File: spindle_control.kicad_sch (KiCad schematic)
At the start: 15 parts, among them U27 EL357N-G, U28 LM358DR

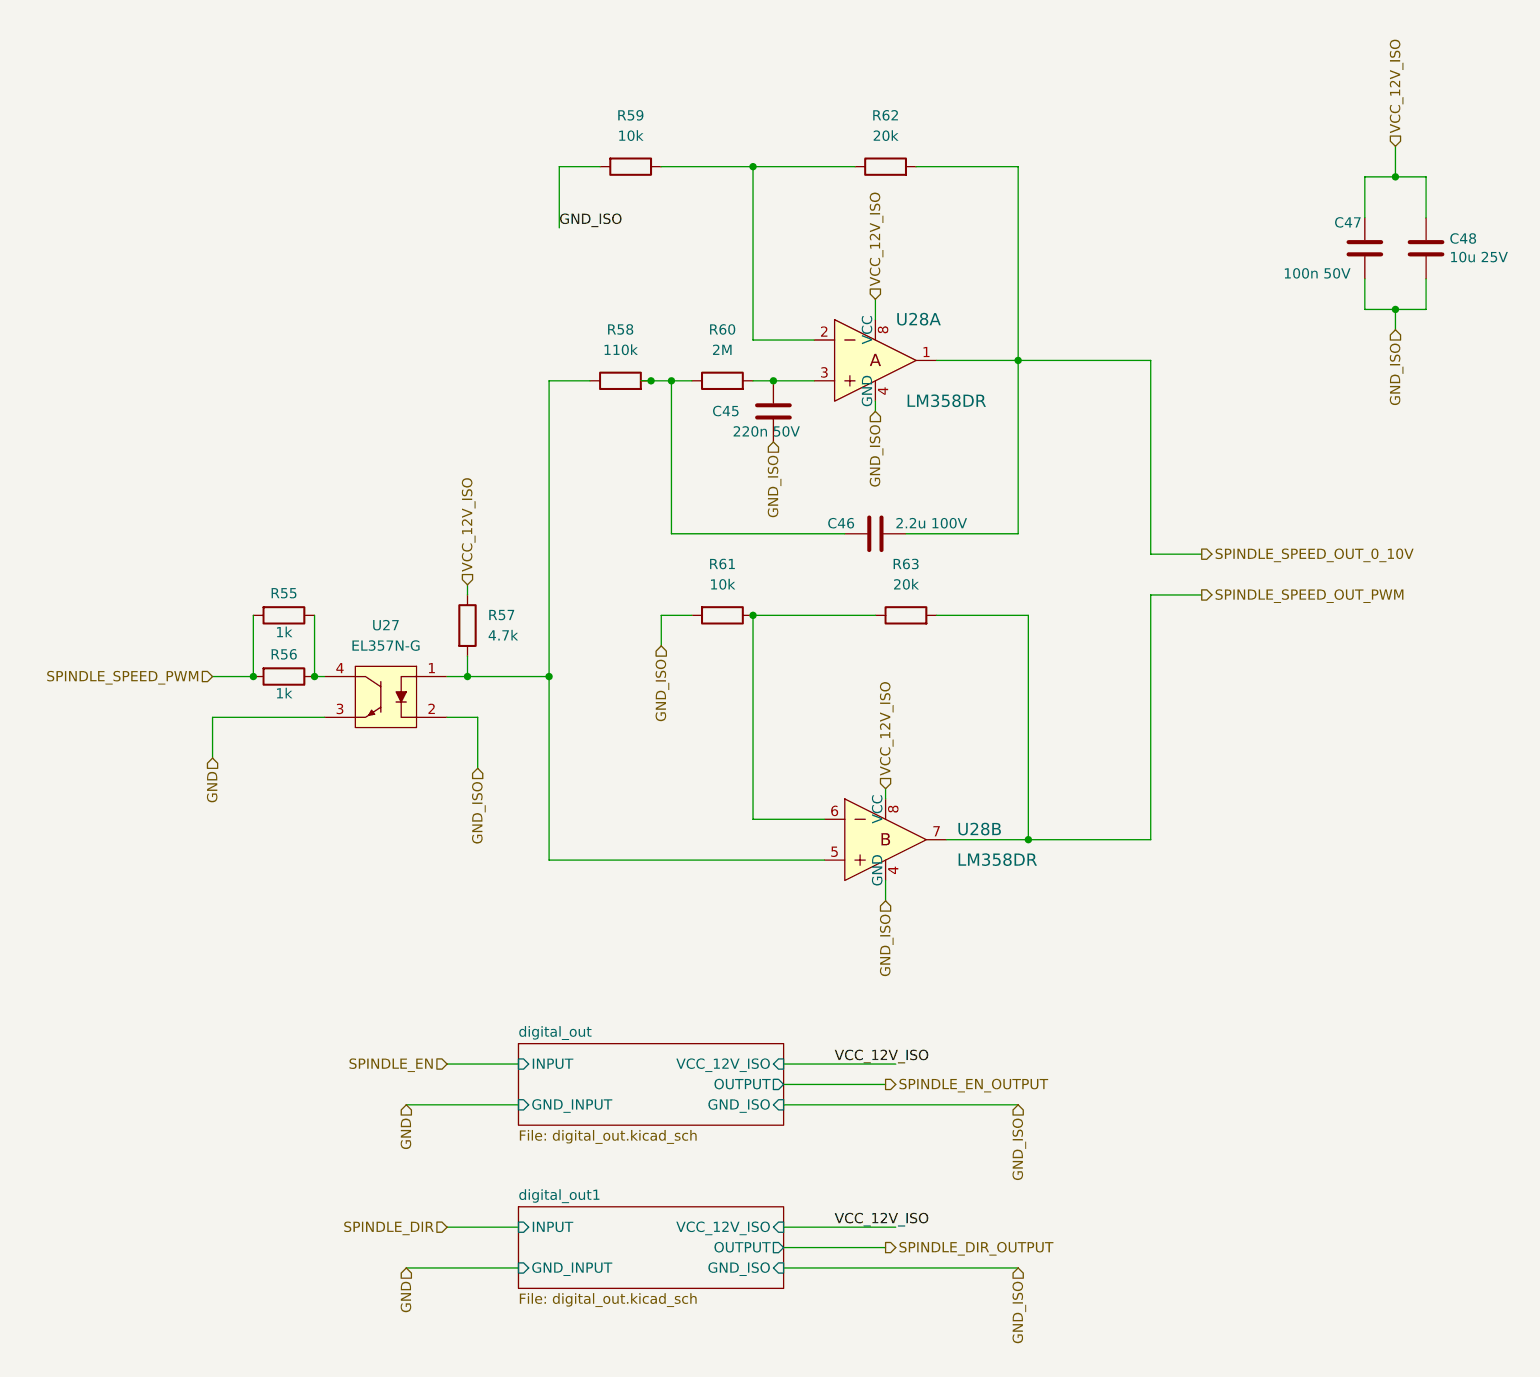
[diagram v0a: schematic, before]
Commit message: Refactored top sheet
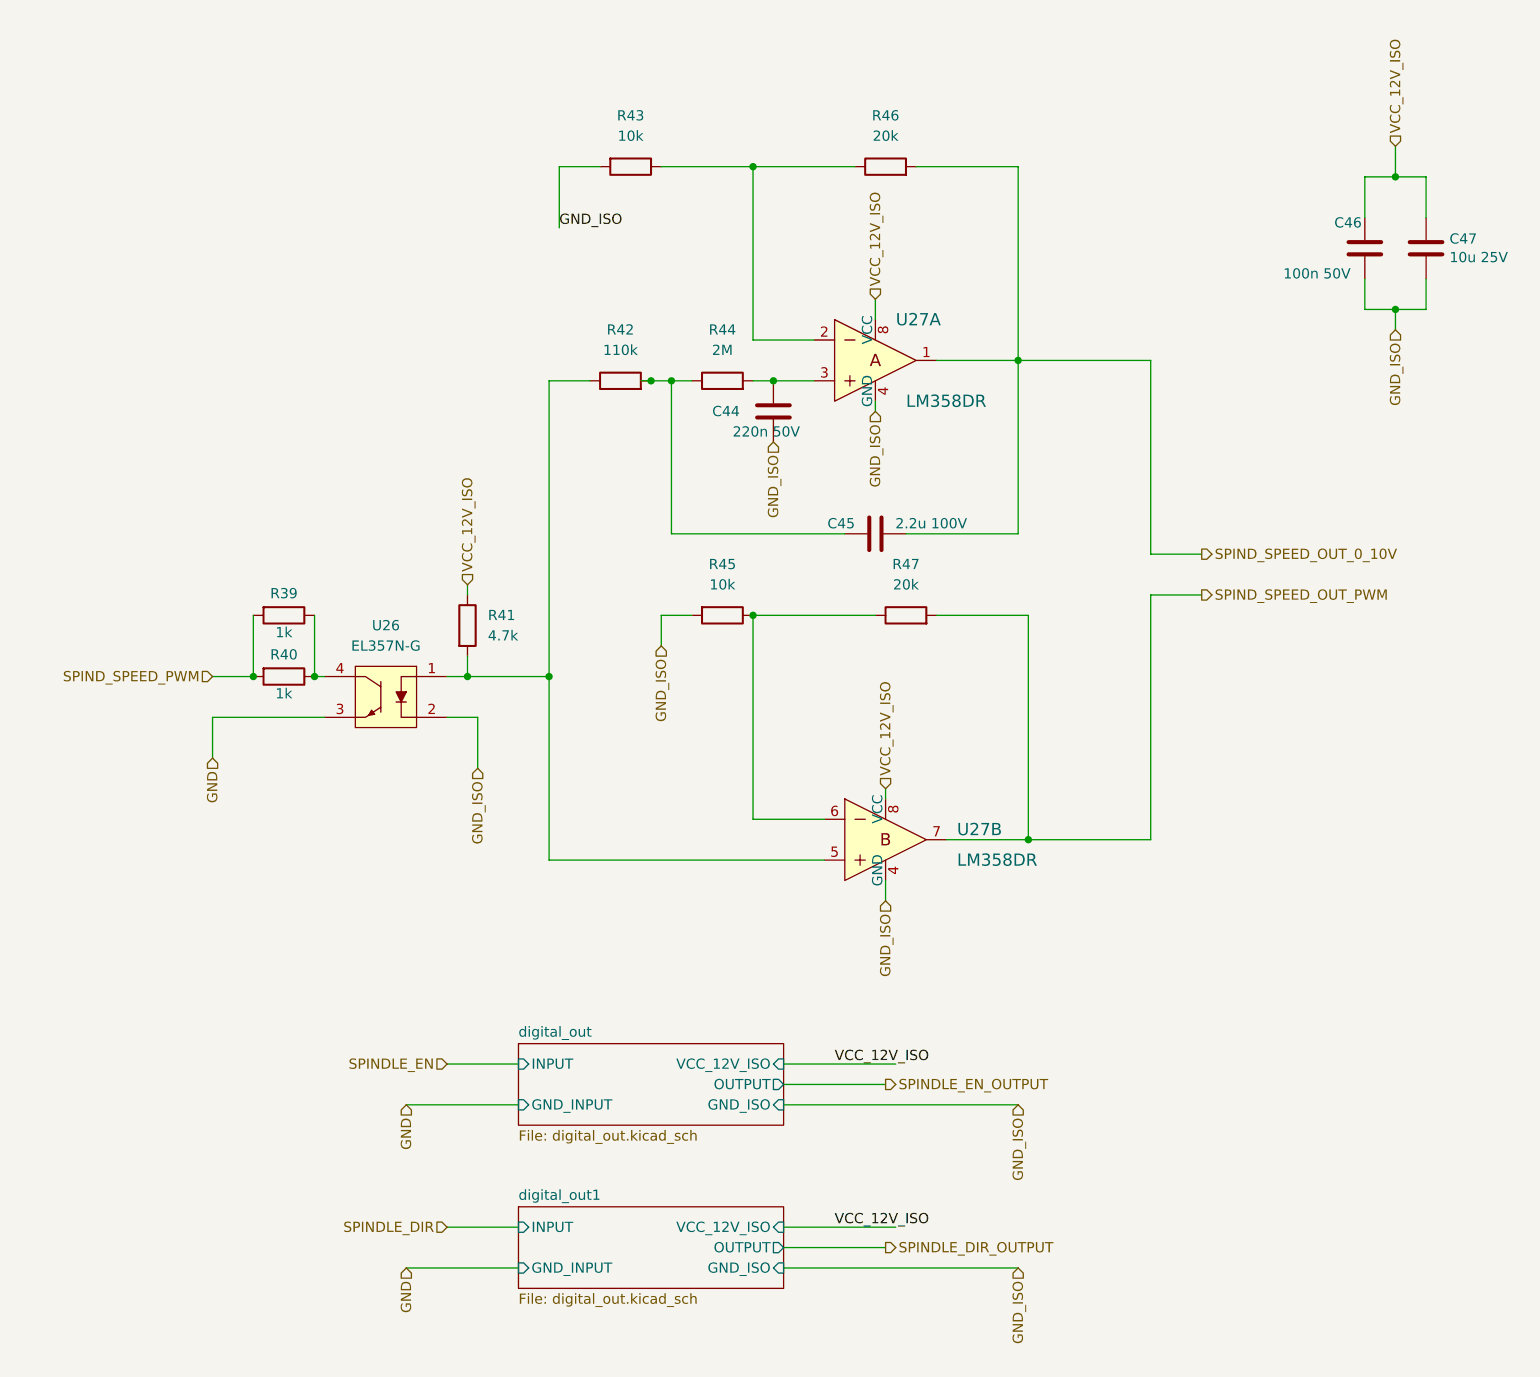
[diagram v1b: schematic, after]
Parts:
- renumbered C45 to C44, C46 to C45, C47 to C46, C48 to C47, R55 to R39, R56 to R40, R57 to R41, R58 to R42, R59 to R43, R60 to R44, R61 to R45, R62 to R46, R63 to R47, U27 to U26, U28 to U27
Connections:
- net SPINDLE_SPEED_OUT_0_10V renamed SPIND_SPEED_OUT_0_10V
- net SPINDLE_SPEED_OUT_PWM renamed SPIND_SPEED_OUT_PWM
- net SPINDLE_SPEED_PWM renamed SPIND_SPEED_PWM
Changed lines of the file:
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@@
     (effects (font (size 1.27 1.27)) (justify right))
   )
-  (hierarchical_label "SPINDLE_SPEED_PWM" (shape input) (at 53.34 93.98 180)
+  (hierarchical_label "SPIND_SPEED_PWM" (shape input) (at 53.34 93.98 180)
     (effects (font (size 1.27 1.27)) (justify right))
   )
@@
     (effects (font (size 1.27 1.27)) (justify right))
   )
-  (hierarchical_label "SPINDLE_SPEED_OUT_0_10V" (shape output) (at 176.53 78.74 0)
+  (hierarchical_label "SPIND_SPEED_OUT_0_10V" (shape output) (at 176.53 78.74 0)
     (effects (font (size 1.27 1.27)) (justify left))
   )
@@
     (effects (font (size 1.27 1.27)) (justify right))
   )
-  (hierarchical_label "SPINDLE_SPEED_OUT_PWM" (shape output) (at 176.53 83.82 0)
+  (hierarchical_label "SPIND_SPEED_OUT_PWM" (shape output) (at 176.53 83.82 0)
     (effects (font (size 1.27 1.27)) (justify left))
   )
   (symbol (lib_id "Device:R") (at 85.09 87.63 0) (unit 1)
     (in_bom yes) (on_board yes) (fields_autoplaced)
-    (property "Reference" "R57" (id 0) (at 87.63 86.3599 0)
+    (property "Reference" "R41" (id 0) (at 87.63 86.3599 0)
       (effects (font (size 1.27 1.27)) (justify left))
     )
@@
   (symbol (lib_id "PersonnalSymbolLibrary:EL357N-G") (at 74.93 96.52 0) (mirror y) (unit 1)
     (in_bom yes) (on_board yes) (fields_autoplaced)
-    (property "Reference" "U27" (id 0) (at 74.93 87.63 0))
+    (property "Reference" "U26" (id 0) (at 74.93 87.63 0))
     (property "Value" "EL357N-G" (id 1) (at 74.93 90.17 0))
     (property "Footprint" "ELM357N-G:SOP254P700X200-4N" (id 2) (at 73.66 101.6 0)
@@
   (symbol (lib_id "Device:R") (at 105.41 30.48 270) (unit 1)
     (in_bom yes) (on_board yes) (fields_autoplaced)
-    (property "Reference" "R59" (id 0) (at 105.41 24.13 90))
+    (property "Reference" "R43" (id 0) (at 105.41 24.13 90))
     (property "Value" "10k" (id 1) (at 105.41 26.67 90))
     (property "Footprint" "Resistor_SMD:R_0402_1005Metric_Pad0.72x0.64mm_HandSolder" (id 2) (at 105.41 28.702 90)
@@
   (symbol (lib_id "Device:R") (at 116.84 57.15 90) (unit 1)
     (in_bom yes) (on_board yes) (fields_autoplaced)
-    (property "Reference" "R60" (id 0) (at 116.84 50.8 90))
+    (property "Reference" "R44" (id 0) (at 116.84 50.8 90))
     (property "Value" "2M" (id 1) (at 116.84 53.34 90))
     (property "Footprint" "Resistor_SMD:R_0603_1608Metric" (id 2) (at 116.84 58.928 90)
@@
   (symbol (lib_id "dk_Linear-Amplifiers-Instrumentation-OP-Amps-Buffer-Amps:LM358DR") (at 135.89 54.61 0) (unit 1)
     (in_bom yes) (on_board yes)
-    (property "Reference" "U28" (id 0) (at 138.43 49.53 0)
+    (property "Reference" "U27" (id 0) (at 138.43 49.53 0)
       (effects (font (size 1.524 1.524)) (justify left))
     )
@@
   (symbol (lib_id "Device:R") (at 62.23 86.36 270) (unit 1)
     (in_bom yes) (on_board yes)
-    (property "Reference" "R55" (id 0) (at 62.23 83.6422 90))
+    (property "Reference" "R39" (id 0) (at 62.23 83.6422 90))
     (property "Value" "1k" (id 1) (at 62.23 88.4936 90))
     (property "Footprint" "Resistor_SMD:R_1206_3216Metric" (id 2) (at 62.23 84.582 90)
@@
   (symbol (lib_id "Device:R") (at 116.84 86.36 270) (unit 1)
     (in_bom yes) (on_board yes) (fields_autoplaced)
-    (property "Reference" "R61" (id 0) (at 116.84 80.01 90))
+    (property "Reference" "R45" (id 0) (at 116.84 80.01 90))
     (property "Value" "10k" (id 1) (at 116.84 82.55 90))
     (property "Footprint" "Resistor_SMD:R_0402_1005Metric_Pad0.72x0.64mm_HandSolder" (id 2) (at 116.84 84.582 90)
@@
   (symbol (lib_id "Device:R") (at 104.14 57.15 90) (unit 1)
     (in_bom yes) (on_board yes) (fields_autoplaced)
-    (property "Reference" "R58" (id 0) (at 104.14 50.8 90))
+    (property "Reference" "R42" (id 0) (at 104.14 50.8 90))
     (property "Value" "110k" (id 1) (at 104.14 53.34 90))
     (property "Footprint" "Resistor_SMD:R_0603_1608Metric" (id 2) (at 104.14 58.928 90)
@@
   (symbol (lib_id "Device:C") (at 123.19 60.96 180) (unit 1)
     (in_bom yes) (on_board yes)
-    (property "Reference" "C45" (id 0) (at 115.57 60.9599 0)
+    (property "Reference" "C44" (id 0) (at 115.57 60.9599 0)
       (effects (font (size 1.27 1.27)) (justify right))
     )
@@
   (symbol (lib_id "Device:C") (at 196.85 40.64 0) (unit 1)
     (in_bom yes) (on_board yes)
-    (property "Reference" "C47" (id 0) (at 193.04 37.4649 0)
+    (property "Reference" "C46" (id 0) (at 193.04 37.4649 0)
       (effects (font (size 1.27 1.27)) (justify left))
     )
@@
   (symbol (lib_id "Device:C") (at 135.89 76.2 90) (unit 1)
     (in_bom yes) (on_board yes)
-    (property "Reference" "C46" (id 0) (at 133.3499 74.93 90)
+    (property "Reference" "C45" (id 0) (at 133.3499 74.93 90)
       (effects (font (size 1.27 1.27)) (justify left))
     )
@@
   (symbol (lib_id "Device:R") (at 139.7 86.36 90) (unit 1)
     (in_bom yes) (on_board yes) (fields_autoplaced)
-    (property "Reference" "R63" (id 0) (at 139.7 80.01 90))
+    (property "Reference" "R47" (id 0) (at 139.7 80.01 90))
     (property "Value" "20k" (id 1) (at 139.7 82.55 90))
     (property "Footprint" "Resistor_SMD:R_0805_2012Metric" (id 2) (at 139.7 88.138 90)
@@
   (symbol (lib_id "Device:R") (at 62.23 93.98 270) (unit 1)
     (in_bom yes) (on_board yes)
-    (property "Reference" "R56" (id 0) (at 62.23 91.2622 90))
+    (property "Reference" "R40" (id 0) (at 62.23 91.2622 90))
     (property "Value" "1k" (id 1) (at 62.23 96.1136 90))
     (property "Footprint" "Resistor_SMD:R_1206_3216Metric" (id 2) (at 62.23 92.202 90)
@@
   (symbol (lib_id "Device:R") (at 137.16 30.48 90) (unit 1)
     (in_bom yes) (on_board yes) (fields_autoplaced)
-    (property "Reference" "R62" (id 0) (at 137.16 24.13 90))
+    (property "Reference" "R46" (id 0) (at 137.16 24.13 90))
     (property "Value" "20k" (id 1) (at 137.16 26.67 90))
     (property "Footprint" "Resistor_SMD:R_0805_2012Metric" (id 2) (at 137.16 32.258 90)
@@
   (symbol (lib_id "dk_Linear-Amplifiers-Instrumentation-OP-Amps-Buffer-Amps:LM358DR") (at 137.16 114.3 0) (unit 2)
     (in_bom yes) (on_board yes) (fields_autoplaced)
-    (property "Reference" "U28" (id 0) (at 146.05 113.03 0)
+    (property "Reference" "U27" (id 0) (at 146.05 113.03 0)
       (effects (font (size 1.524 1.524)) (justify left))
     )
@@
   (symbol (lib_id "Device:C") (at 204.47 40.64 0) (unit 1)
     (in_bom yes) (on_board yes)
-    (property "Reference" "C48" (id 0) (at 207.391 39.4716 0)
-      (effects (font (size 1.27 1.27)) (justify left))
-    )
+    (property "Reference" "C47" (id 0) (at 207.391 39.4716 0)
+      (effects (font (size 1.27 1.27)) (justify left))
+    )
